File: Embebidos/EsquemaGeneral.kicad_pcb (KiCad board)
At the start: 2 copper layers, 100 x 99.9 mm, 79 parts, among them IC1 ESP32-WROVER-B__8MB_, J1 USB_A, J2 Conn_01x02, J3 RJ45, J4 RJ45, J5 Conn_02x06_Counter_Clockwise, J6 Conn_01x08, J7 Conn_01x04, Q1 BC847, Q2 BC847, Q3 BSS138, Q4 DMP3056LSDQ-13, Q5 BSS138, Q6 DMP3056LSDQ-13, SW1 SW_Reset, SW2 SW_Boot, U2 LM358, U3 SPX3819M5-L-3-3, U4 MIC29302WU, U5 MIC5219-3.3YM5

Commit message: Cambio huella Capacitor
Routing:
- net +3.3V: track 1457.2 -> 1452.3 mm
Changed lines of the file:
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@@
   )
   (segment (start 146.2718 51.3379) (end 149.3468 51.3379) (width 1) (layer "F.Cu") (net 1))
+  (segment (start 138 57.47) (end 138.09 57.38) (width 1) (layer "F.Cu") (net 1))
   (segment (start 150.8 57.56) (end 149.4747 57.56) (width 0.6) (layer "F.Cu") (net 1))
   (segment (start 133.2341 66.6345) (end 128.7446 62.145) (width 0.6) (layer "F.Cu") (net 1))
@@
   (segment (start 103.6182 127.9071) (end 103.7987 127.9071) (width 0.6) (layer "F.Cu") (net 1))
   (segment (start 144.3961 62.72) (end 145.2964 63.6203) (width 0.6) (layer "F.Cu") (net 1))
-  (segment (start 138.6934 60.0028) (end 139.0259 59.6703) (width 1) (layer "F.Cu") (net 1))
   (segment (start 104.53 109.92) (end 104.4811 109.9689) (width 1) (layer "F.Cu") (net 1))
   (segment (start 144.5764 80.412) (end 145.5484 79.44) (width 1) (layer "F.Cu") (net 1))
@@
   (segment (start 132.1648 61.645) (end 122.775 61.645) (width 0.6) (layer "F.Cu") (net 1))
   (segment (start 119.81 53.14) (end 119.81 54.7153) (width 0.6) (layer "F.Cu") (net 1))
-  (segment (start 133.8025 57.7375) (end 133.8025 58.3263) (width 1) (layer "F.Cu") (net 1))
   (segment (start 119.59 123.535) (end 118.5147 123.535) (width 0.25) (layer "F.Cu") (net 1))
   (segment (start 80.53 87.55) (end 80.8908 87.9108) (width 1) (layer "F.Cu") (net 1))
@@
   (segment (start 150.8 60.1) (end 149.4747 60.1) (width 0.6) (layer "F.Cu") (net 1))
   (segment (start 93.3 53.1468) (end 93.3 52.5621) (width 0.6) (layer "F.Cu") (net 1))
+  (segment (start 134.07 57.47) (end 138 57.47) (width 1) (layer "F.Cu") (net 1))
   (segment (start 128.2475 102.0844) (end 128.2475 105.68) (width 0.6) (layer "F.Cu") (net 1))
   (segment (start 145.5484 79.44) (end 146.5994 78.389) (width 1) (layer "F.Cu") (net 1))
   (segment (start 144.3961 62.72) (end 144.3961 61.0941) (width 0.6) (layer "F.Cu") (net 1))
-  (segment (start 139.0259 59.6703) (end 139.0259 56.4259) (width 1) (layer "F.Cu") (net 1))
   (segment (start 117.2175 104.5371) (end 116.7348 104.0544) (width 0.6) (layer "F.Cu") (net 1))
   (segment (start 110.8411 46.9289) (end 112.4887 46.9289) (width 0.6) (layer "F.Cu") (net 1))
@@
   (segment (start 147.3243 85.1567) (end 138.4988 93.9822) (width 0.6) (layer "F.Cu") (net 1))
   (segment (start 147.6257 55.02) (end 150.8 55.02) (width 0.6) (layer "F.Cu") (net 1))
-  (segment (start 133.8025 58.3263) (end 135.479 60.0028) (width 1) (layer "F.Cu") (net 1))
   (segment (start 145.3264 74.1286) (end 145.0461 73.8483) (width 0.6) (layer "F.Cu") (net 1))
   (segment (start 166.1322 52.48) (end 167.8 52.48) (width 0.6) (layer "F.Cu") (net 1))
@@
   (segment (start 95.2701 49.5999) (end 92.03 52.84) (width 0.6) (layer "F.Cu") (net 1))
   (segment (start 90.76 55.38) (end 90.0899 55.38) (width 1) (layer "F.Cu") (net 1))
-  (segment (start 139.0259 56.4259) (end 138.09 55.49) (width 1) (layer "F.Cu") (net 1))
   (segment (start 128.2475 102.0844) (end 129.841 102.0844) (width 0.6) (layer "F.Cu") (net 1))
   (segment (start 90.0899 55.38) (end 84.3246 61.1453) (width 1) (layer "F.Cu") (net 1))
@@
   (segment (start 84.3246 65.902) (end 84.4879 66.0653) (width 1) (layer "F.Cu") (net 1))
   (segment (start 120.4964 75.9917) (end 141.1814 75.9917) (width 0.6) (layer "F.Cu") (net 1))
+  (segment (start 133.8025 57.7375) (end 134.07 57.47) (width 1) (layer "F.Cu") (net 1))
   (segment (start 111.9012 50.9624) (end 114.5717 48.2919) (width 0.6) (layer "F.Cu") (net 1))
   (segment (start 85.4 64.145) (end 86.3627 64.145) (width 1) (layer "F.Cu") (net 1))
@@
   (segment (start 135.845 51.71) (end 138.09 53.955) (width 1) (layer "F.Cu") (net 1))
   (segment (start 144.5764 83.4464) (end 144.5764 80.412) (width 1) (layer "F.Cu") (net 1))
-  (segment (start 135.479 60.0028) (end 138.6934 60.0028) (width 1) (layer "F.Cu") (net 1))
+  (segment (start 138.09 57.38) (end 138.09 55.49) (width 1) (layer "F.Cu") (net 1))
   (segment (start 103.263 119.51) (end 114.8024 119.51) (width 1) (layer "F.Cu") (net 1))
   (segment (start 145.5071 54.4324) (end 145.8824 54.4324) (width 0.6) (layer "F.Cu") (net 1))

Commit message: eliminar pistas para volver a intetar
:c
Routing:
- net +3.3V: track 1452.3 -> 0.00 mm, vias 27 -> 0
- net 4.1V: track 322.6 -> 0.00 mm, vias 8 -> 0
- net 3.3Vop2: track 174.8 -> 0.00 mm
- net Net-(IC1-Pad35): track 126.3 -> 0.00 mm
- net /Acondicionamiento/SCK_RFID: track 78.9 -> 0.00 mm, vias 1 -> 0
- net /Acondicionamiento/MISO_RFID: track 78.3 -> 0.00 mm, vias 1 -> 0
- net /Acondicionamiento/CS_RFID: track 77.3 -> 0.00 mm, vias 1 -> 0
- net /Acondicionamiento/RXGPS: track 75.0 -> 0.00 mm, vias 2 -> 0
- net /Acondicionamiento/TXGPS: track 71.6 -> 0.00 mm, vias 2 -> 0
- net /Acondicionamiento/ctr_led_delantero: track 71.3 -> 0.00 mm, vias 2 -> 0
- net /Acondicionamiento/ctr_trasero: track 62.4 -> 0.00 mm
- net /Acondicionamiento/Din_der: track 59.3 -> 0.00 mm, vias 2 -> 0
- net Net-(IC1-Pad34): track 53.8 -> 0.00 mm
- net /USB_UART/DTR: track 48.2 -> 0.00 mm, vias 2 -> 0
- net /Luces traseras/VCC_INF: track 35.3 -> 0.00 mm, vias 1 -> 0
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
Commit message: siiiiiiiiii
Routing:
- net GND: track 0.00 -> 615.0 mm, vias 0 -> 5
- net +3.3V: track 0.00 -> 248.4 mm, vias 0 -> 4
- net +5V: track 0.00 -> 169.7 mm
- net /Acondicionamiento/SDA_PAN: track 0.00 -> 139.4 mm, vias 0 -> 3
- net /Acondicionamiento/SCL_PAN: track 0.00 -> 136.7 mm, vias 0 -> 3
- net 3.3Vop2: track 0.00 -> 133.4 mm, vias 0 -> 1
- net 4.1V: track 0.00 -> 114.1 mm
- net CtrlOnOff: track 0.00 -> 111.7 mm, vias 0 -> 4
- net /Acondicionamiento/MOSI_RFID: track 0.00 -> 91.8 mm, vias 0 -> 1
- net /Acondicionamiento/SCK_RFID: track 0.00 -> 89.3 mm, vias 0 -> 2
- net /Acondicionamiento/CS_RFID: track 0.00 -> 86.1 mm, vias 0 -> 2
- net /Acondicionamiento/MISO_RFID: track 0.00 -> 85.7 mm, vias 0 -> 1
- net /Acondicionamiento/VO_Inf: track 0.00 -> 82.7 mm, vias 0 -> 1
- net /Acondicionamiento/RXGPS: track 0.00 -> 75.0 mm
- net /Acondicionamiento/TXGPS: track 0.00 -> 70.6 mm
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
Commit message: Tierras
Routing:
- net GND: track 615.0 -> 2.10 mm, vias 5 -> 1
- net Net-(R19-Pad2): track 12.6 -> 11.5 mm
- added copper zone on B.Cu, net GND
- added copper zone on F.Cu, net GND

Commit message: arreglo del uart feo y pequeño
Gracias profeee por si acaso lee estooooo
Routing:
- net +3.3V: track 248.4 -> 255.9 mm
- net GND: vias 1 -> 3
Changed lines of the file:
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@@
     (property "Sheetfile" "USB_UART.kicad_sch")
     (property "Sheetname" "USB_UART")
+    (clearance 0.2)
     (attr smd)
     (fp_text reference "U1" (at -0.25427 -3.43257 90) (layer "F.SilkS")
@@
       (net 59 "/USB_UART/D-") (pinfunction "D-") (pintype "bidirectional"))
     (pad "5" smd roundrect locked (at -1.955 0.75 270) (size 0.81 0.26) (layers "F.Cu" "F.Paste" "F.Mask") (roundrect_rratio 0.01)
-      (net 1 "+3.3V") (pinfunction "VIO") (pintype "power_in"))
+      (net 1 "+3.3V") (pinfunction "VIO") (pintype "power_in") (clearance 0.2))
     (pad "6" smd roundrect locked (at -1.955 1.25 270) (size 0.81 0.26) (layers "F.Cu" "F.Paste" "F.Mask") (roundrect_rratio 0.01)
       (net 1 "+3.3V") (pinfunction "VDD") (pintype "power_in"))
@@
       (net 111 "unconnected-(U1-Pad24)") (pinfunction "~{DCD}") (pintype "input+no_connect"))
     (pad "25" smd rect locked (at 0 0 270) (size 2.68 2.68) (layers "F.Cu" "F.Mask")
-      (net 2 "GND") (pinfunction "GND") (pintype "passive"))
+      (net 2 "GND") (pinfunction "GND") (pintype "passive") (clearance 0.2))
   )
   (footprint "Capacitor_Tantalum_SMD:CP_EIA-6032-28_Kemet-C_Pad2.25x2.35mm_HandSolder" (layer "F.Cu")
@@
       (effects (font (size 1 1) (thickness 0.15)))
     )
-    (fp_line (start -3.315 14.08) (end 12.205 14.08) (layer "F.SilkS") (width 0.12))
-    (fp_line (start 12.205 -3.88) (end 12.205 14.08) (layer "F.SilkS") (width 0.12))
+    (fp_line (start -3.315 10) (end 12.205 10) (layer "F.SilkS") (width 0.12))
+    (fp_line (start 12.205 -3.88) (end 12.205 10) (layer "F.SilkS") (width 0.12))
     (fp_line (start -4 0.5) (end -3.5 0) (layer "F.SilkS") (width 0.12))
-    (fp_line (start -3.315 -3.88) (end -3.315 14.08) (layer "F.SilkS") (width 0.12))
+    (fp_line (start -3.315 -3.88) (end -3.315 10) (layer "F.SilkS") (width 0.12))
     (fp_line (start -3.5 0) (end -4 -0.5) (layer "F.SilkS") (width 0.12))
     (fp_line (start 12.205 -3.88) (end -3.315 -3.88) (layer "F.SilkS") (width 0.12))
     (fp_line (start -4 -0.5) (end -4 0.5) (layer "F.SilkS") (width 0.12))
-    (fp_line (start 12.6 14.47) (end 12.6 -4.27) (layer "F.CrtYd") (width 0.05))
-    (fp_line (start 12.6 14.47) (end -3.71 14.47) (layer "F.CrtYd") (width 0.05))
+    (fp_line (start 12.6 11) (end 12.6 -4.27) (layer "F.CrtYd") (width 0.05))
+    (fp_line (start 12.6 11) (end -3.71 11) (layer "F.CrtYd") (width 0.05))
     (fp_line (start -3.71 -4.27) (end 12.6 -4.27) (layer "F.CrtYd") (width 0.05))
-    (fp_line (start -3.71 -4.27) (end -3.71 14.47) (layer "F.CrtYd") (width 0.05))
+    (fp_line (start -3.71 -4.27) (end -3.71 11) (layer "F.CrtYd") (width 0.05))
     (fp_line (start -3.205 -2.77) (end -2.205 -3.77) (layer "F.Fab") (width 0.12))
     (fp_line (start -2.205 -3.77) (end 12.095 -3.77) (layer "F.Fab") (width 0.12))
-    (fp_line (start 12.095 13.97) (end -3.205 13.97) (layer "F.Fab") (width 0.12))
-    (fp_line (start -3.205 13.97) (end -3.205 -2.77) (layer "F.Fab") (width 0.12))
-    (fp_line (start 12.095 -3.77) (end 12.095 13.97) (layer "F.Fab") (width 0.12))
+    (fp_line (start 12.095 10) (end -3.205 10) (layer "F.Fab") (width 0.12))
+    (fp_line (start -3.205 10) (end -3.205 -2.77) (layer "F.Fab") (width 0.12))
+    (fp_line (start 12.095 -3.77) (end 12.095 10) (layer "F.Fab") (width 0.12))
     (pad "" np_thru_hole circle (at -1.27 6.35) (size 3.2 3.2) (drill 3.2) (layers *.Cu *.Mask))
     (pad "" np_thru_hole circle (at 10.16 6.35) (size 3.2 3.2) (drill 3.2) (layers *.Cu *.Mask))
@@
   (segment (start 110.53 60.205) (end 114.155 60.205) (width 1) (layer "F.Cu") (net 1))
   (segment (start 136.28 71.2202) (end 137.1134 71.2202) (width 1) (layer "F.Cu") (net 1))
+  (segment (start 120.07 59.44) (end 119.57 59.44) (width 0.25) (layer "F.Cu") (net 1))
+  (segment (start 115.12 59.31) (end 118.03 59.31) (width 1) (layer "F.Cu") (net 1))
   (segment (start 135.91 71.2202) (end 136.28 71.2202) (width 1) (layer "F.Cu") (net 1))
   (segment (start 144.1144 83.3429) (end 144.1144 82.3517) (width 1) (layer "F.Cu") (net 1))
@@
   (segment (start 104.53 109.92) (end 102.11 109.92) (width 1) (layer "F.Cu") (net 1))
   (segment (start 142.37 51.21) (end 150.8 51.21) (width 1) (layer "F.Cu") (net 1))
+  (segment (start 119.44 59.31) (end 118.03 59.31) (width 0.25) (layer "F.Cu") (net 1))
   (segment (start 84.7371 83.3429) (end 144.1144 83.3429) (width 1) (layer "F.Cu") (net 1))
   (segment (start 138.8359 50.0577) (end 141.1791 52.4009) (width 1) (layer "F.Cu") (net 1))
@@
   (segment (start 114.155 60.205) (end 114.19 60.24) (width 1) (layer "F.Cu") (net 1))
   (segment (start 144.1144 82.3517) (end 144.1144 80.874) (width 1) (layer "F.Cu") (net 1))
+  (segment (start 119.57 59.44) (end 119.44 59.31) (width 0.25) (layer "F.Cu") (net 1))
   (segment (start 90.0049 58.7596) (end 109.0846 58.7596) (width 1) (layer "F.Cu") (net 1))
   (segment (start 135.845 51.71) (end 135.945 51.61) (width 1) (layer "F.Cu") (net 1))
+  (segment (start 118.03 59.31) (end 118.865 60.145) (width 0.25) (layer "F.Cu") (net 1))
   (segment (start 137.2063 50.0577) (end 138.8359 50.0577) (width 1) (layer "F.Cu") (net 1))
   (segment (start 133.12 51.71) (end 135.845 51.71) (width 1) (layer "F.Cu") (net 1))
+  (segment (start 114.19 60.24) (end 115.12 59.31) (width 1) (layer "F.Cu") (net 1))
   (segment (start 109.0846 58.7596) (end 110.53 60.205) (width 1) (layer "F.Cu") (net 1))
   (segment (start 93.5992 108.5767) (end 89.8323 112.3436) (width 1) (layer "F.Cu") (net 1))
@@
   (segment (start 99.44 136.57) (end 99.44 138.61) (width 0.25) (layer "F.Cu") (net 2))
   (segment (start 99.44 138.61) (end 99.48 138.65) (width 0.25) (layer "F.Cu") (net 2))
+  (via (at 143.11 118.12) (size 0.8) (drill 0.4) (layers "F.Cu" "B.Cu") (free) (net 2))
+  (via (at 120.07 60.72) (size 0.8) (drill 0.4) (layers "F.Cu" "B.Cu") (net 2))
   (via (at 99.44 136.57) (size 0.8) (drill 0.4) (layers "F.Cu" "B.Cu") (net 2))
   (segment (start 139.2186 63.7186) (end 145.2964 63.7186) (width 0.6) (layer "F.Cu") (net 3))

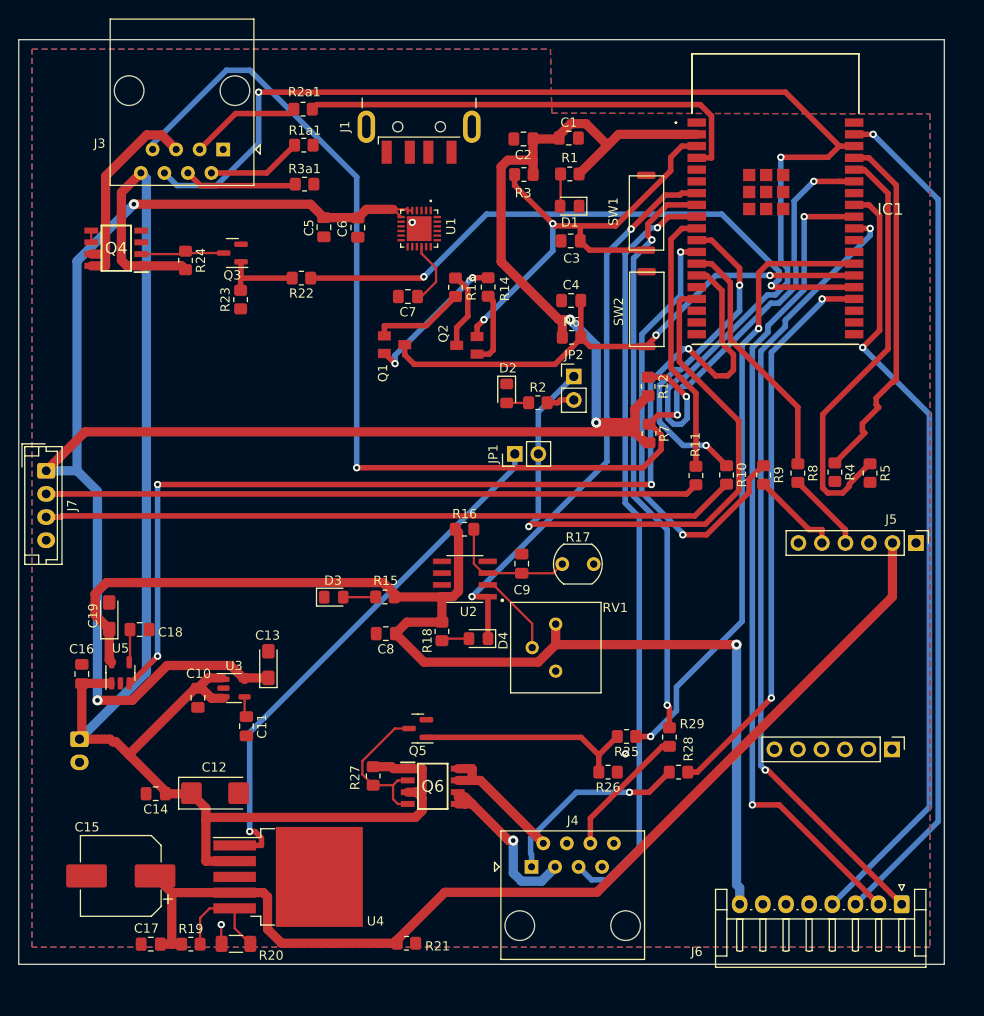
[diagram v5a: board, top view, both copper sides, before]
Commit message: arreglo serigrafias y rutas
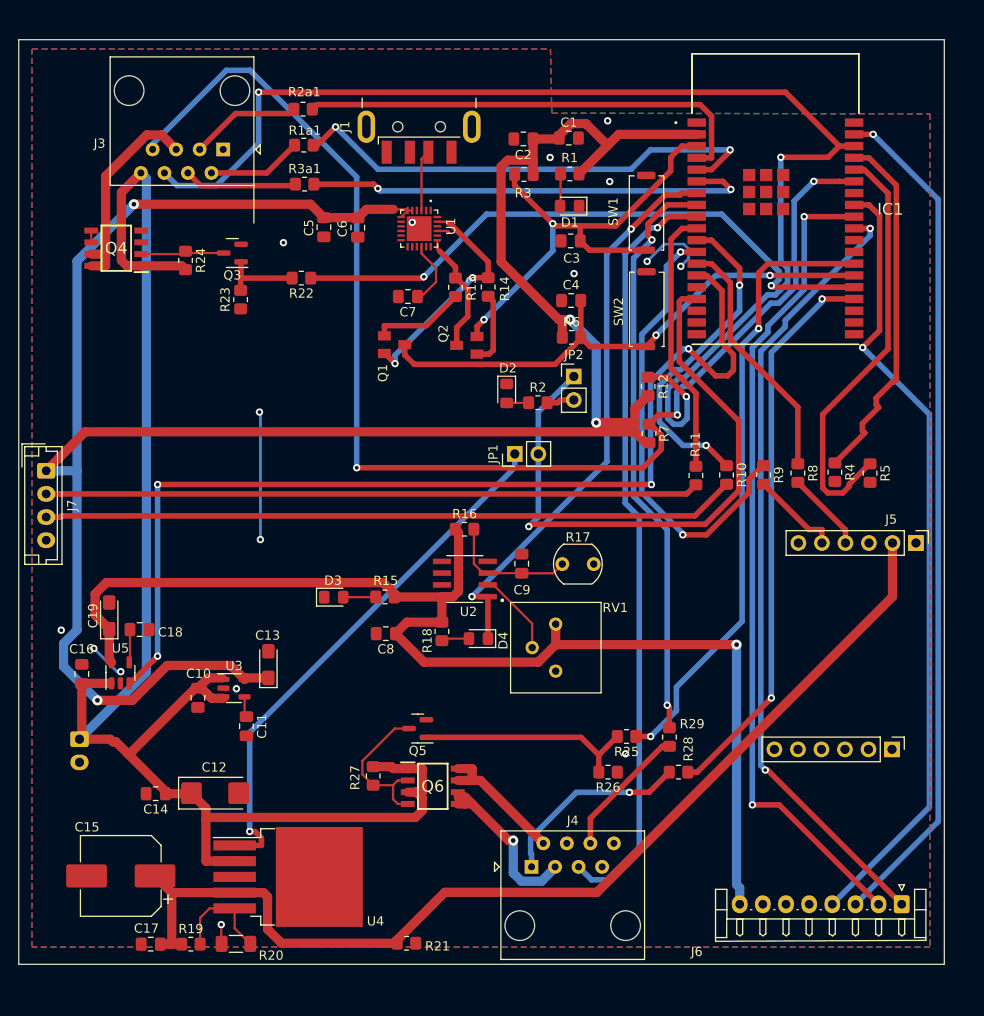
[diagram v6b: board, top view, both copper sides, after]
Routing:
- net /Acondicionamiento/UP_stk: track 0.00 -> 53.2 mm, vias 0 -> 2
- net /Acondicionamiento/RHT_stk: track 0.00 -> 49.5 mm, vias 0 -> 2
- net GND: track 2.10 -> 27.6 mm, vias 3 -> 16
- net /USB_UART/DTR: track 16.0 -> 25.0 mm
- net /USB_UART/D+: track 0.00 -> 6.61 mm
- net /USB_UART/RTS: track 8.37 -> 13.3 mm
- net /Acondicionamiento/RXCP: track 0.00 -> 1.33 mm
- net +3.3V: track 255.9 -> 256.9 mm

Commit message: queda un error
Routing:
- net /Acondicionamiento/RXCP: track 1.33 -> 254.2 mm, vias 0 -> 2
- net /Acondicionamiento/TXCP: track 0.00 -> 120.7 mm, vias 0 -> 2
- net GND: track 27.6 -> 57.3 mm, vias 16 -> 19
- net VBUS: track 0.00 -> 14.3 mm, vias 0 -> 2
- net /USB_UART/D-: track 0.00 -> 6.61 mm
- net /Acondicionamiento/Din_der: track 61.2 -> 64.0 mm
- net /Acondicionamiento/CS_RFID: track 86.1 -> 87.8 mm
- net 3.3Vop2: track 133.4 -> 135.0 mm
- net /Acondicionamiento/SCK_RFID: track 89.3 -> 90.7 mm
- net /Acondicionamiento/LDR_IN: track 61.8 -> 63.1 mm
- net /Acondicionamiento/UP_stk: track 53.2 -> 54.0 mm
- net /Acondicionamiento/ctr_led_delantero: track 67.0 -> 67.6 mm

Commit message: Operacion salvar
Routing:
- net /Acondicionamiento/RXCP: track 254.2 -> 1.45 mm, vias 2 -> 0
- net /Acondicionamiento/TXCP: track 120.7 -> 0.98 mm, vias 2 -> 0
- net GND: track 57.3 -> 27.6 mm, vias 19 -> 16
- net VBUS: track 14.3 -> 0.88 mm, vias 2 -> 0
- net /USB_UART/D-: track 6.61 -> 1.22 mm
- net /USB_UART/D+: track 6.61 -> 2.33 mm
- net /Acondicionamiento/Din_der: track 64.0 -> 61.2 mm
- net /Acondicionamiento/CS_RFID: track 87.8 -> 86.1 mm
- net 3.3Vop2: track 135.0 -> 133.4 mm
- net +3.3V: track 256.9 -> 258.4 mm
- net /Acondicionamiento/SCK_RFID: track 90.7 -> 89.3 mm
- net /Acondicionamiento/LDR_IN: track 63.1 -> 61.8 mm
- net /Acondicionamiento/UP_stk: track 54.0 -> 53.2 mm
- net /Acondicionamiento/ctr_led_delantero: track 67.6 -> 67.0 mm
